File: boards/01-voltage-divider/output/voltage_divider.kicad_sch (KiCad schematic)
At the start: 4 parts, among them J1 IN, J2 OUT

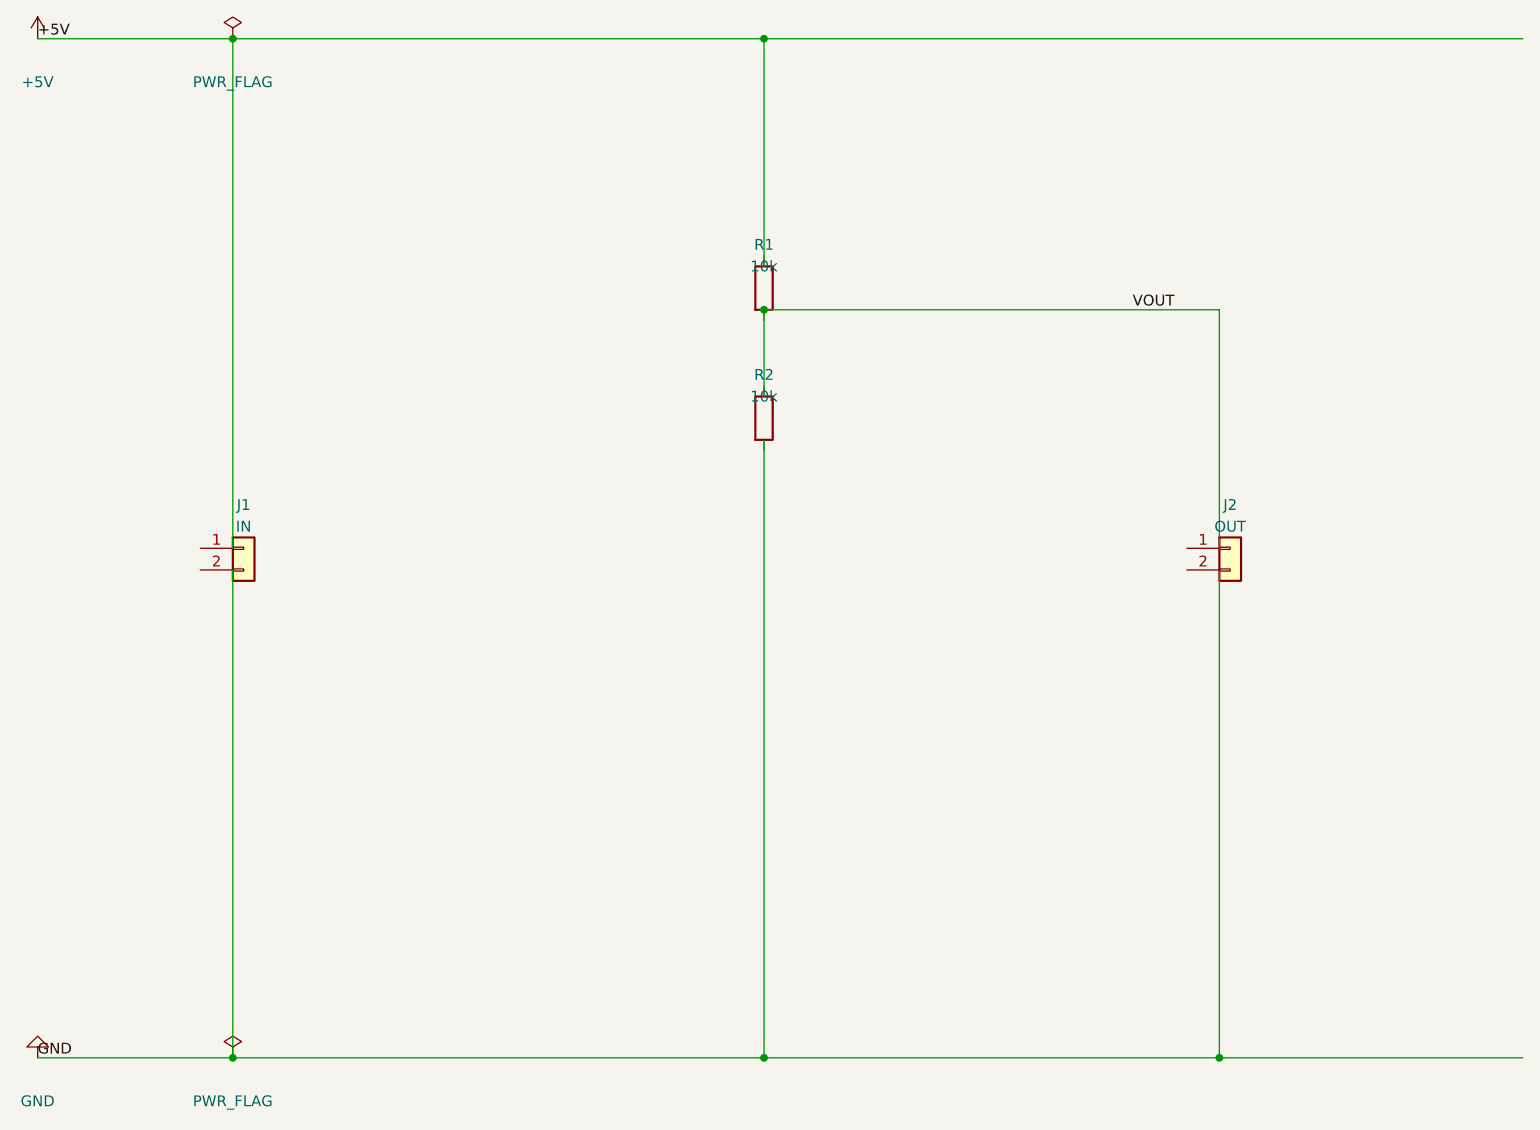
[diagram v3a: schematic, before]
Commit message: fix(schematic): Remove floating wire endpoints in voltage divider
The VIN and GND power rails were extending to x=199.39mm (X_RIGHT)
but no components connected that far right. The rightmost connections
are R1 (x=110.49mm) for VIN and J2 (x=165.10mm) for GND.

Fix: Only extend rails to their rightmost actual connection points
instead of an arbitrary X_RIGHT boundary. This eliminates the
floating wire endpoints that caused ERC warnings.

Before: 2 floating_wire errors, 2 ERC warnings
After: No errors, no warnings

Closes #725

Co-Authored-By: Claude Opus 4.5 <noreply@anthropic.com>
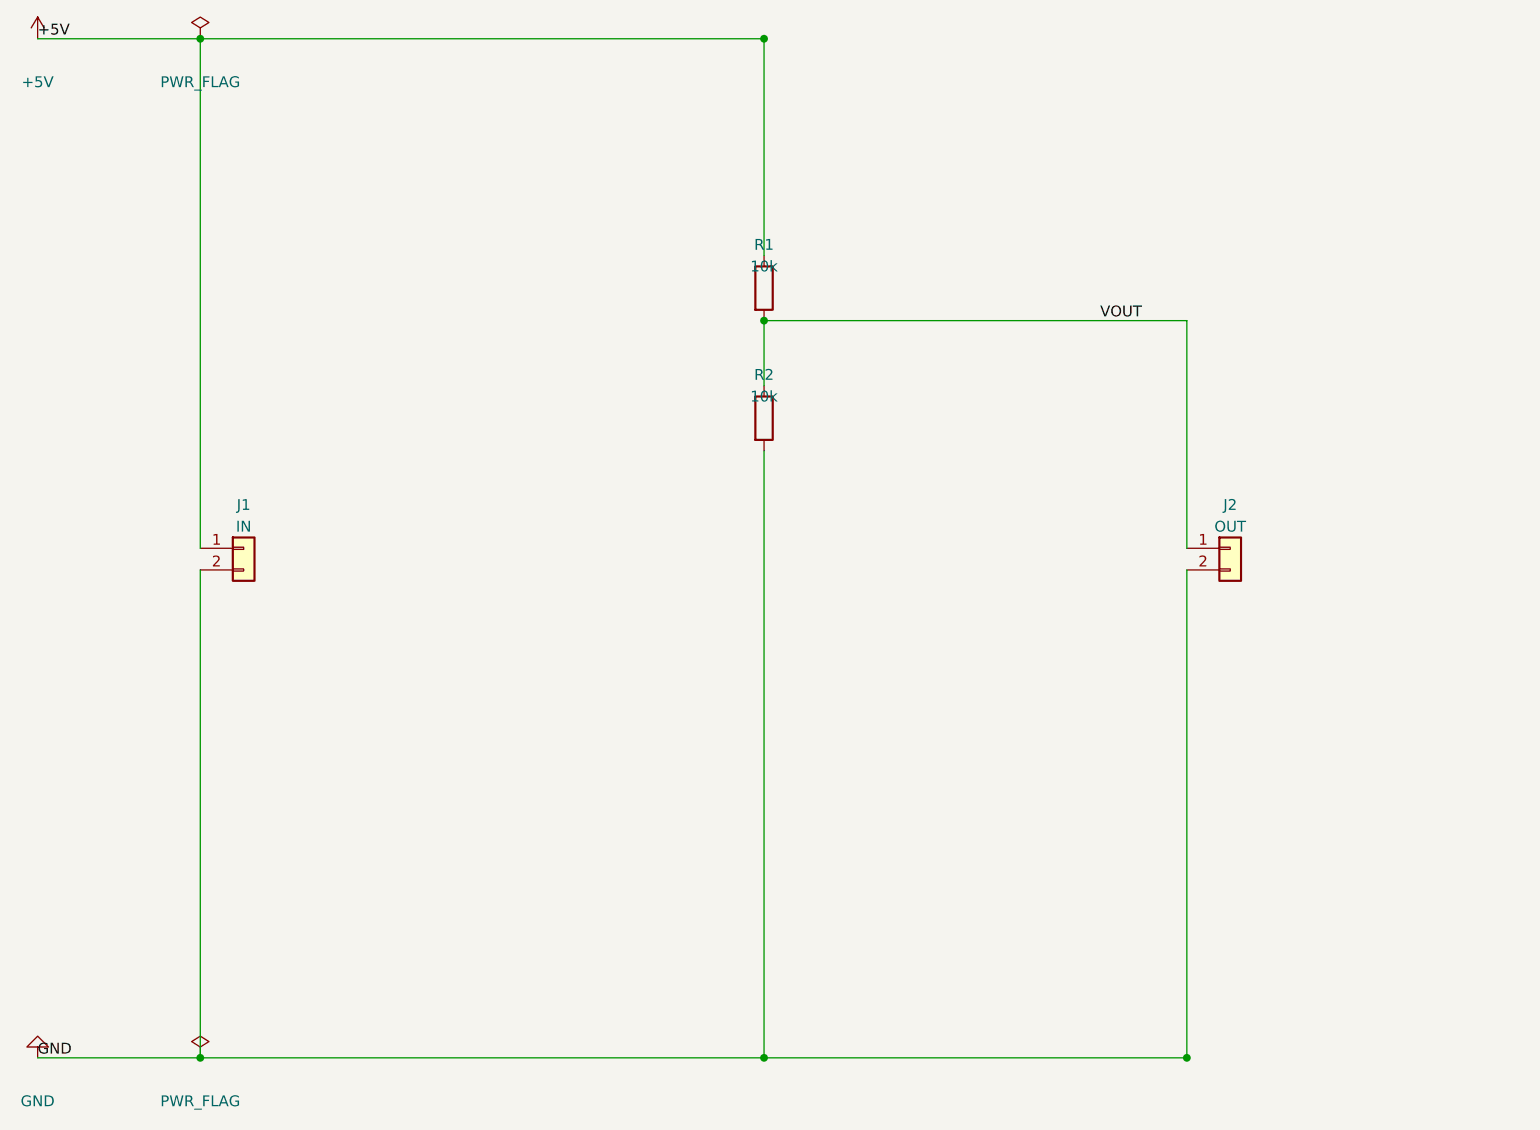
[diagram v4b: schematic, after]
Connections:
- net +5V: now also J1.1 (Pin_1), R1.1
- net GND: now also J1.2 (Pin_2), J2.2 (Pin_2), R2.2
- net VOUT: now also J2.1 (Pin_1), R1.2, R2.1
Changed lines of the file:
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@@
     (instances
       (project "project"
-        (path "/f6577161-ce3c-4d5c-9281-2bb1198b1d2d" (reference "J1") (unit 1)
+        (path "/f248c599-1edb-428b-92f1-1714e73d748a" (reference "J1") (unit 1)
         )
       )
@@
     (instances
       (project "project"
-        (path "/f6577161-ce3c-4d5c-9281-2bb1198b1d2d" (reference "R1") (unit 1)
+        (path "/f248c599-1edb-428b-92f1-1714e73d748a" (reference "R1") (unit 1)
         )
       )
@@
     (instances
       (project "project"
-        (path "/f6577161-ce3c-4d5c-9281-2bb1198b1d2d" (reference "R2") (unit 1)
+        (path "/f248c599-1edb-428b-92f1-1714e73d748a" (reference "R2") (unit 1)
         )
       )
@@
     (instances
       (project "project"
-        (path "/f6577161-ce3c-4d5c-9281-2bb1198b1d2d" (reference "J2") (unit 1)
+        (path "/f248c599-1edb-428b-92f1-1714e73d748a" (reference "J2") (unit 1)
         )
       )
@@
     (instances
       (project "project"
-        (path "/f6577161-ce3c-4d5c-9281-2bb1198b1d2d" (reference "#PWR01") (unit 1)
+        (path "/f248c599-1edb-428b-92f1-1714e73d748a" (reference "#PWR01") (unit 1)
         )
       )
@@
     (instances
       (project "project"
-        (path "/f6577161-ce3c-4d5c-9281-2bb1198b1d2d" (reference "#PWR02") (unit 1)
+        (path "/f248c599-1edb-428b-92f1-1714e73d748a" (reference "#PWR02") (unit 1)
         )
       )
@@
   (symbol
     (lib_id "power:PWR_FLAG")
-    (at 48.26 30.48 0)
+    (at 44.45 30.48 0)
     (unit 1)
     (exclude_from_sim no)
@@
     (dnp no)
     (property "Reference" "#PWR03"
-      (at 48.26 33.02 0)
+      (at 44.45 33.02 0)
       (effects
         (font
@@
     )
     (property "Value" "PWR_FLAG"
-      (at 48.26 35.56 0)
+      (at 44.45 35.56 0)
       (effects
         (font
@@
     )
     (property "Footprint" ""
-      (at 48.26 30.48 0)
+      (at 44.45 30.48 0)
       (effects
         (font
@@
     )
     (property "Datasheet" ""
-      (at 48.26 30.48 0)
-      (effects
-        (font
-          (size 1.27 1.27)
-        )
-        (hide yes)
-      )
-    )
-    (pin "1"
-    )
-    (instances
-      (project "project"
-        (path "/f6577161-ce3c-4d5c-9281-2bb1198b1d2d" (reference "#PWR03") (unit 1)
+      (at 44.45 30.48 0)
+      (effects
+        (font
+          (size 1.27 1.27)
+        )
+        (hide yes)
+      )
+    )
+    (pin "1"
+    )
+    (instances
+      (project "project"
+        (path "/f248c599-1edb-428b-92f1-1714e73d748a" (reference "#PWR03") (unit 1)
         )
       )
@@
   (symbol
     (lib_id "power:PWR_FLAG")
-    (at 48.26 149.86 0)
+    (at 44.45 149.86 0)
     (unit 1)
     (exclude_from_sim no)
@@
     (dnp no)
     (property "Reference" "#PWR04"
-      (at 48.26 152.4 0)
+      (at 44.45 152.4 0)
       (effects
         (font
@@
     )
     (property "Value" "PWR_FLAG"
-      (at 48.26 154.94 0)
+      (at 44.45 154.94 0)
       (effects
         (font
@@
     )
     (property "Footprint" ""
-      (at 48.26 149.86 0)
+      (at 44.45 149.86 0)
       (effects
         (font
@@
     )
     (property "Datasheet" ""
-      (at 48.26 149.86 0)
-      (effects
-        (font
-          (size 1.27 1.27)
-        )
-        (hide yes)
-      )
-    )
-    (pin "1"
-    )
-    (instances
-      (project "project"
-        (path "/f6577161-ce3c-4d5c-9281-2bb1198b1d2d" (reference "#PWR04") (unit 1)
-        )
-      )
-    )
-  )
-  (wire
-    (pts (xy 25.4 30.48) (xy 48.26 30.48))
-    (stroke
-      (width 0)
-      (type default)
-    )
-  )
-  (wire
-    (pts (xy 48.26 30.48) (xy 110.49 30.48))
-    (stroke
-      (width 0)
-      (type default)
-    )
-  )
-  (wire
-    (pts (xy 110.49 30.48) (xy 199.39 30.48))
-    (stroke
-      (width 0)
-      (type default)
-    )
-  )
-  (wire
-    (pts (xy 25.4 149.86) (xy 48.26 149.86))
-    (stroke
-      (width 0)
-      (type default)
-    )
-  )
-  (wire
-    (pts (xy 48.26 149.86) (xy 110.49 149.86))
-    (stroke
-      (width 0)
-      (type default)
-    )
-  )
-  (wire
-    (pts (xy 110.49 149.86) (xy 163.83 149.86))
-    (stroke
-      (width 0)
-      (type default)
-    )
-  )
-  (wire
-    (pts (xy 163.83 149.86) (xy 199.39 149.86))
-    (stroke
-      (width 0)
-      (type default)
-    )
-  )
-  (wire
-    (pts (xy 48.26 90.17) (xy 48.26 30.48))
-    (stroke
-      (width 0)
-      (type default)
-    )
-  )
-  (wire
-    (pts (xy 48.26 92.71) (xy 48.26 149.86))
-    (stroke
-      (width 0)
-      (type default)
-    )
-  )
-  (wire
-    (pts (xy 110.49 57.15) (xy 110.49 30.48))
-    (stroke
-      (width 0)
-      (type default)
-    )
-  )
-  (wire
-    (pts (xy 110.49 62.23) (xy 110.49 72.39))
-    (stroke
-      (width 0)
-      (type default)
-    )
-  )
-  (wire
-    (pts (xy 110.49 77.47) (xy 110.49 149.86))
-    (stroke
-      (width 0)
-      (type default)
-    )
-  )
-  (wire
-    (pts (xy 110.49 62.23) (xy 163.83 62.23))
-    (stroke
-      (width 0)
-      (type default)
-    )
-  )
-  (wire
-    (pts (xy 163.83 62.23) (xy 163.83 90.17))
-    (stroke
-      (width 0)
-      (type default)
-    )
-  )
-  (wire
-    (pts (xy 163.83 92.71) (xy 163.83 149.86))
+      (at 44.45 149.86 0)
+      (effects
+        (font
+          (size 1.27 1.27)
+        )
+        (hide yes)
+      )
+    )
+    (pin "1"
+    )
+    (instances
+      (project "project"
+        (path "/f248c599-1edb-428b-92f1-1714e73d748a" (reference "#PWR04") (unit 1)
+        )
+      )
+    )
+  )
+  (wire
+    (pts (xy 25.4 30.48) (xy 44.45 30.48))
+    (stroke
+      (width 0)
+      (type default)
+    )
+  )
+  (wire
+    (pts (xy 44.45 30.48) (xy 110.49 30.48))
+    (stroke
+      (width 0)
+      (type default)
+    )
+  )
+  (wire
+    (pts (xy 25.4 149.86) (xy 44.45 149.86))
+    (stroke
+      (width 0)
+      (type default)
+    )
+  )
+  (wire
+    (pts (xy 44.45 149.86) (xy 110.49 149.86))
+    (stroke
+      (width 0)
+      (type default)
+    )
+  )
+  (wire
+    (pts (xy 110.49 149.86) (xy 160.02 149.86))
+    (stroke
+      (width 0)
+      (type default)
+    )
+  )
+  (wire
+    (pts (xy 44.45 90.17) (xy 44.45 30.48))
+    (stroke
+      (width 0)
+      (type default)
+    )
+  )
+  (wire
+    (pts (xy 44.45 92.71) (xy 44.45 149.86))
+    (stroke
+      (width 0)
+      (type default)
+    )
+  )
+  (wire
+    (pts (xy 110.49 55.88) (xy 110.49 30.48))
+    (stroke
+      (width 0)
+      (type default)
+    )
+  )
+  (wire
+    (pts (xy 110.49 63.5) (xy 110.49 71.12))
+    (stroke
+      (width 0)
+      (type default)
+    )
+  )
+  (wire
+    (pts (xy 110.49 78.74) (xy 110.49 149.86))
+    (stroke
+      (width 0)
+      (type default)
+    )
+  )
+  (wire
+    (pts (xy 110.49 63.5) (xy 160.02 63.5))
+    (stroke
+      (width 0)
+      (type default)
+    )
+  )
+  (wire
+    (pts (xy 160.02 63.5) (xy 160.02 90.17))
+    (stroke
+      (width 0)
+      (type default)
+    )
+  )
+  (wire
+    (pts (xy 160.02 92.71) (xy 160.02 149.86))
     (stroke
       (width 0)
@@
   )
   (junction
-    (at 48.26 30.48)
+    (at 44.45 30.48)
     (diameter 0)
   )
   (junction
-    (at 48.26 149.86)
+    (at 44.45 149.86)
     (diameter 0)
   )
@@
   )
   (junction
-    (at 110.49 62.23)
+    (at 110.49 63.5)
     (diameter 0)
   )
@@
   )
   (junction
-    (at 163.83 149.86)
+    (at 160.02 149.86)
     (diameter 0)
   )
@@
   )
   (label "VOUT"
-    (at 153.67 62.23 0)
+    (at 149.86 63.5 0)
     (fields_autoplaced yes)
     (effects
@@
   )
   (sheet_instances
-    (path "/f6577161-ce3c-4d5c-9281-2bb1198b1d2d" (page "1")
-    )
-  )
+    (path "/f248c599-1edb-428b-92f1-1714e73d748a" (page "1")
+    )
+  )
